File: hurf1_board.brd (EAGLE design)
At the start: 160 x 100 mm, 32 parts, among them IC1 STM32F10XCXT6, J1 0R, J2 0R, X1 MINI-USB-32005-201, Y1 8MHz

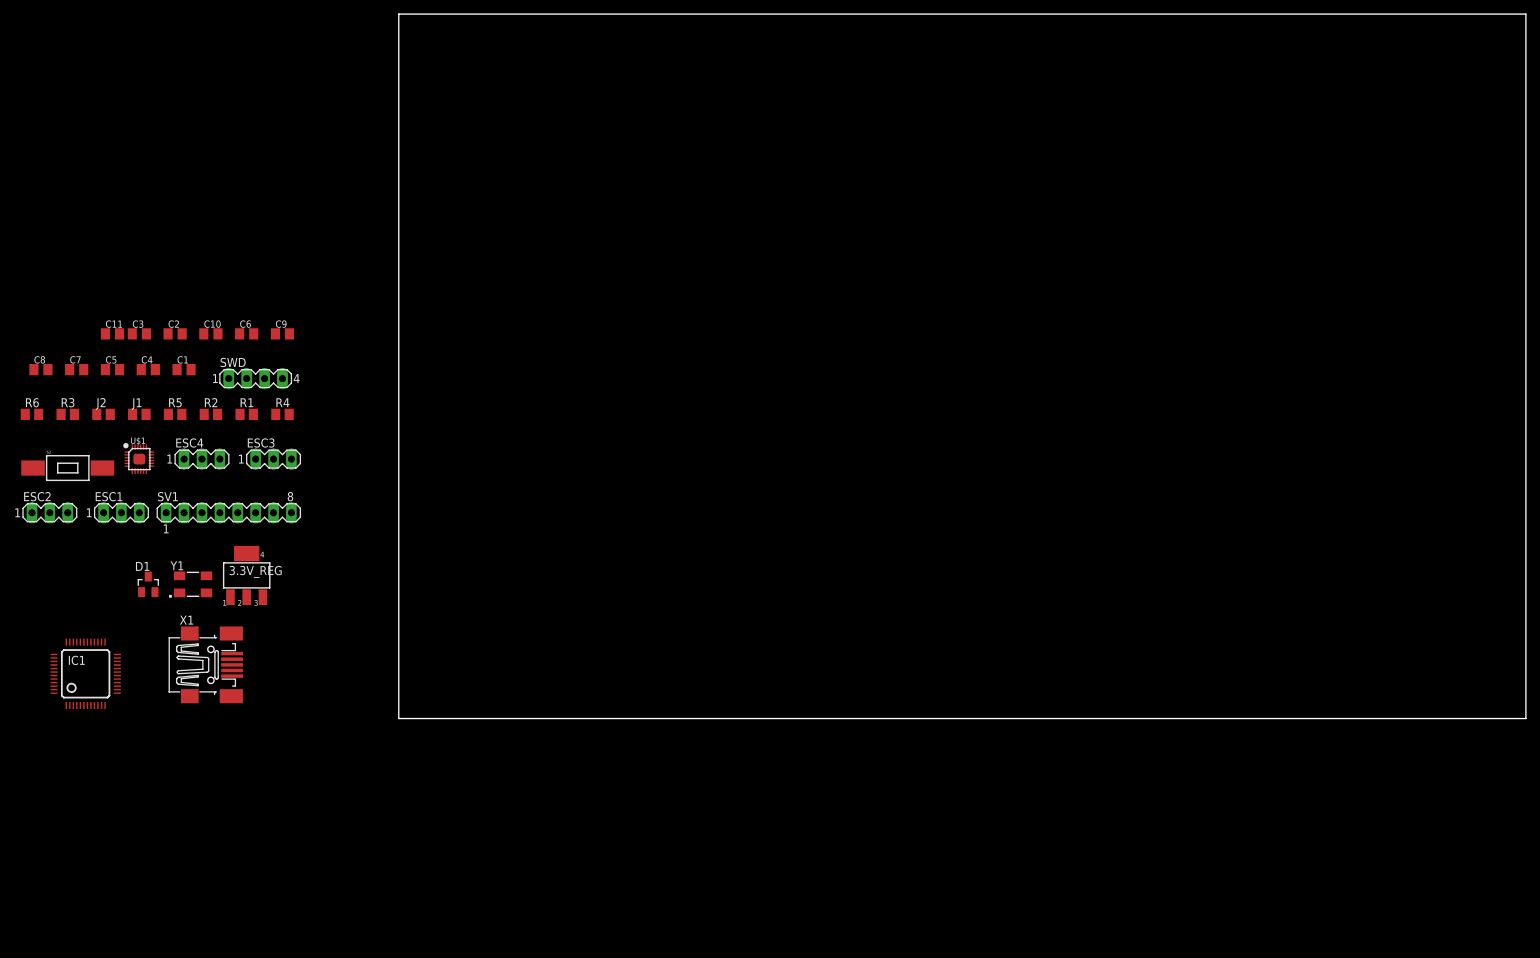
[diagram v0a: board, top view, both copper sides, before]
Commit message: Schematic Completed -schematic w1 -board w1 -controlboard sketch added (.dxf) =.gitignore updated = hurf1_schematic.sch -> hurf1_board.sch = board images added
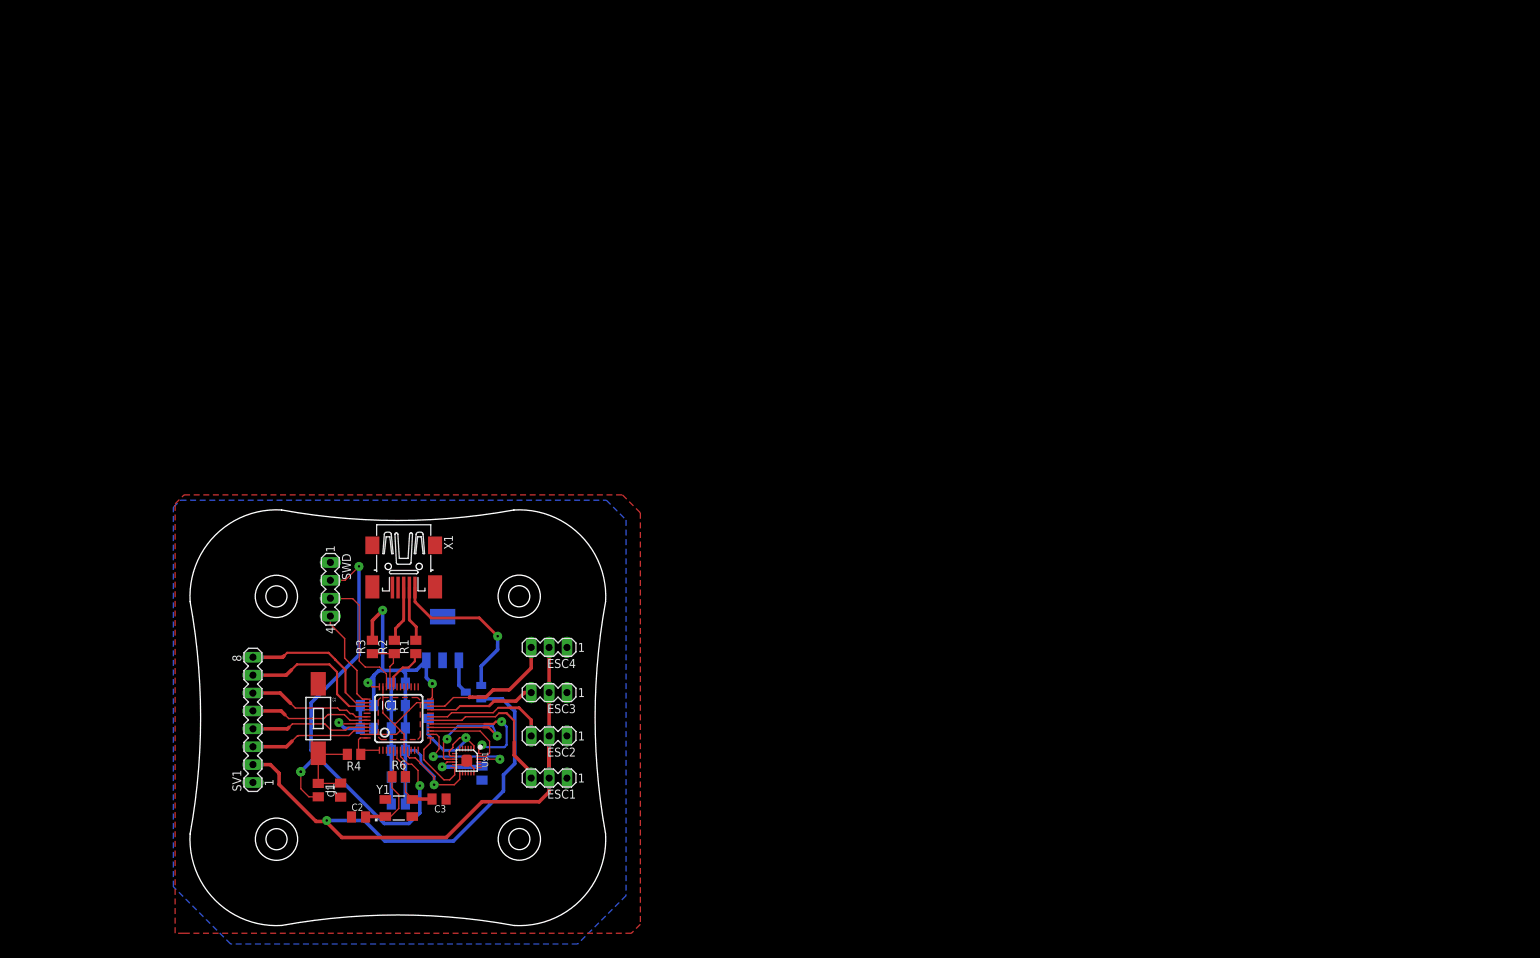
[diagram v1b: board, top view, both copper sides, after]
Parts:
- moved C8 79.8 mm to (-0.06, -12.1), flipped to the bottom, turned to 180 degrees
- moved C3 78.6 mm to (5.71, -11.4), turned to 180 degrees
- moved ESC2 77.6 mm to (21.3, -2.48), turned to 180 degrees
- moved C4 74.3 mm to (11.8, -7.75), flipped to the bottom, turned to 270 degrees
- moved C7 73.7 mm to (-0.06, -8.32), flipped to the bottom, turned to 180 degrees
- moved C2 73.4 mm to (-5.71, -14.0)
- moved R6 73.2 mm to (0.00, -8.26)
- moved ESC1 71.4 mm to (21.3, -8.45), turned to 180 degrees
- moved C11 69.1 mm to (-0.06, -1.33), flipped to the bottom, turned to 180 degrees
- moved C5 67.6 mm to (-0.06, -4.51), flipped to the bottom
- moved C1 63.7 mm to (-8.26, -10.2), turned to 90 degrees
- moved U$1 63.2 mm to (9.65, -5.97), turned to 270 degrees
- moved C6 59.5 mm to (4.19, 1.02), flipped to the bottom, turned to 270 degrees
- moved C10 59.1 mm to (-0.06, 1.84), flipped to the bottom, turned to 180 degrees
- moved J1 59.1 mm to (-11.4, -10.2), turned to 270 degrees
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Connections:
- net SPI1_SS renamed SPI1_NSS
- net USB_N renamed USB_DM
- net USB_P renamed USB_DP
- net ESC1: now also IC1.18
- net ESC2: now also IC1.19
- net ESC3: now also IC1.21
- net ESC4: now also IC1.22
- net MPU_INT: now also IC1.13
- net RC_IN1: now also IC1.46
- net RC_IN2: now also IC1.45
- net RC_IN3: now also IC1.43
- net RC_IN4: now also IC1.42
- net RC_IN5: now also IC1.39
- net RC_IN6: now also IC1.38
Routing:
- net UNREG_5V: track 0.00 -> 123.3 mm, vias 0 -> 1
- net 3.3V: track 0.00 -> 97.4 mm, vias 0 -> 4
- net NRST: track 0.00 -> 73.0 mm, vias 0 -> 4
- net GND: track 0.00 -> 43.3 mm
- net USB_UNREG: track 0.00 -> 23.7 mm, vias 0 -> 1
- net SPI1_MISO: track 0.00 -> 23.5 mm, vias 0 -> 2
- net ESC1: track 0.00 -> 21.9 mm
- net RC_IN6: track 0.00 -> 21.3 mm
- net RC_IN5: track 0.00 -> 21.1 mm
- net ESC4: track 0.00 -> 19.5 mm
- net SPI1_MOSI: track 0.00 -> 19.0 mm, vias 0 -> 2
- net SWDIO: track 0.00 -> 18.9 mm
- net ESC2: track 0.00 -> 17.8 mm
- net VDDIO: track 0.00 -> 17.7 mm, vias 0 -> 1
- net RC_IN4: track 0.00 -> 17.6 mm
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- added copper zone on layer 1, net GND
- added copper zone on layer 16, net GND
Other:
- board size 160 x 100 mm -> 59 x 59 mm

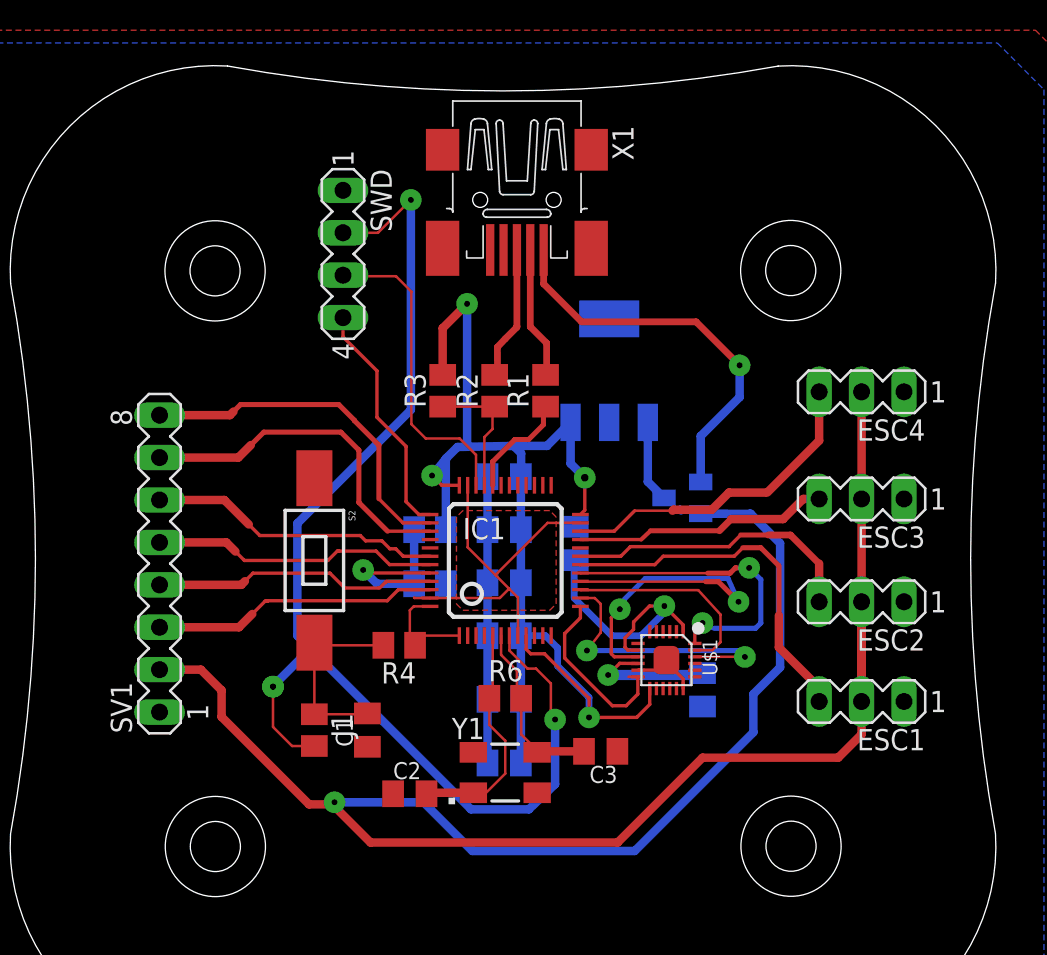
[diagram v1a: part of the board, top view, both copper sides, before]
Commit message: Circuit Size Shrinked -schematic w1 (updated) -board w1s1 (updated)  *SMD Package changed from 0805 -> 0603  *SWD Port changed from DIL -> JST-SH  X UNREG_5V pin must be connected to diode
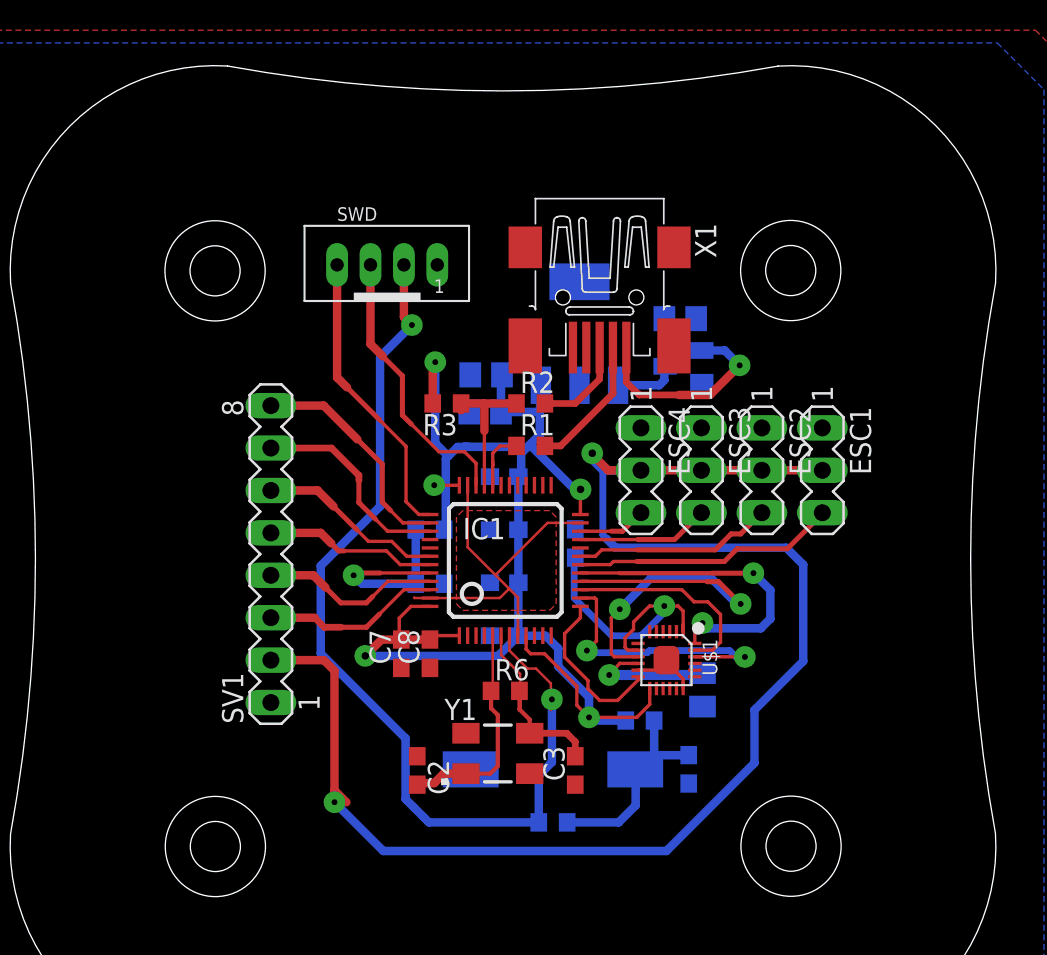
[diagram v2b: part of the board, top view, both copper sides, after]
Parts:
- added C12, C13, C14: 10uF, rcl:C0805
- C1, C10, C11, C2, C3, C5, C6, C7, C8, C9: device resistor:C0805K -> rcl:C0603
- J1, J2, R1, R2, R3, R4, R5, R6: device adafruit:M0805 -> rcl:R0603
- SWD: device con-lstb:MA04-1 -> SRG:JST_B4B-PH_HEADER
- moved C1 19.4 mm to (11.0, -12.5), flipped to the bottom
- moved S2 19.0 mm to (2.86, -12.5), flipped to the bottom, turned to 180 degrees
- moved J1 15.3 mm to (2.86, -15.7), flipped to the bottom, turned to 0 degrees
- moved R4 15.1 mm to (8.06, -9.59), flipped to the bottom
- moved ESC1 14.0 mm to (19.0, 5.40), turned to 270 degrees
- moved ESC4 14.0 mm to (8.13, 5.40), turned to 270 degrees
- moved ESC2 9.88 mm to (15.4, 5.40), turned to 270 degrees
- moved ESC3 9.74 mm to (11.7, 5.40), turned to 270 degrees
- moved C8 7.91 mm to (-4.51, -5.59), flipped to the top, turned to 90 degrees
- moved D1 7.87 mm to (10.7, 11.6)
- moved X1 7.66 mm to (5.65, 15.7)
- moved C7 6.74 mm to (-6.22, -5.59), flipped to the top, turned to 90 degrees
- moved SV1 6.69 mm to (-14.0, 0.38)
- moved R1 3.42 mm to (1.52, 6.86), turned to 0 degrees
- moved 3.3V_REG 2.85 mm to (4.45, 13.6)
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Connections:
- net 3.3V: now also C12.1, C13.1
- net GND: now also C12.2, C13.2, C14.2, SWD.P1; no longer SWD.1
- net N$4: now also C14.1
- net NRST: now also SWD.P2; no longer SWD.2
- net SWDCLK: now also SWD.P4; no longer SWD.4
- net SWDIO: now also SWD.P3; no longer SWD.3
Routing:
- net UNREG_5V: track 123.3 -> 88.3 mm, vias 1 -> 2
- net GND: track 43.3 -> 26.1 mm
- net ESC4: track 19.5 -> 4.09 mm
- net NRST: track 73.0 -> 59.2 mm, vias 4 -> 2
- net USB_UNREG: track 23.7 -> 12.5 mm
- net RC_IN5: track 21.1 -> 12.5 mm
- net RC_IN6: track 21.3 -> 13.8 mm
- net ESC3: track 15.3 -> 7.91 mm
- net N$2: track 12.7 -> 5.77 mm
- net RC_IN3: track 17.2 -> 10.4 mm
- net RC_IN4: track 17.6 -> 11.2 mm
- net RC_IN1: track 17.1 -> 10.7 mm
- net RC_IN2: track 17.0 -> 10.8 mm
- net ESC1: track 21.9 -> 15.8 mm
- net ESC2: track 17.8 -> 11.9 mm
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
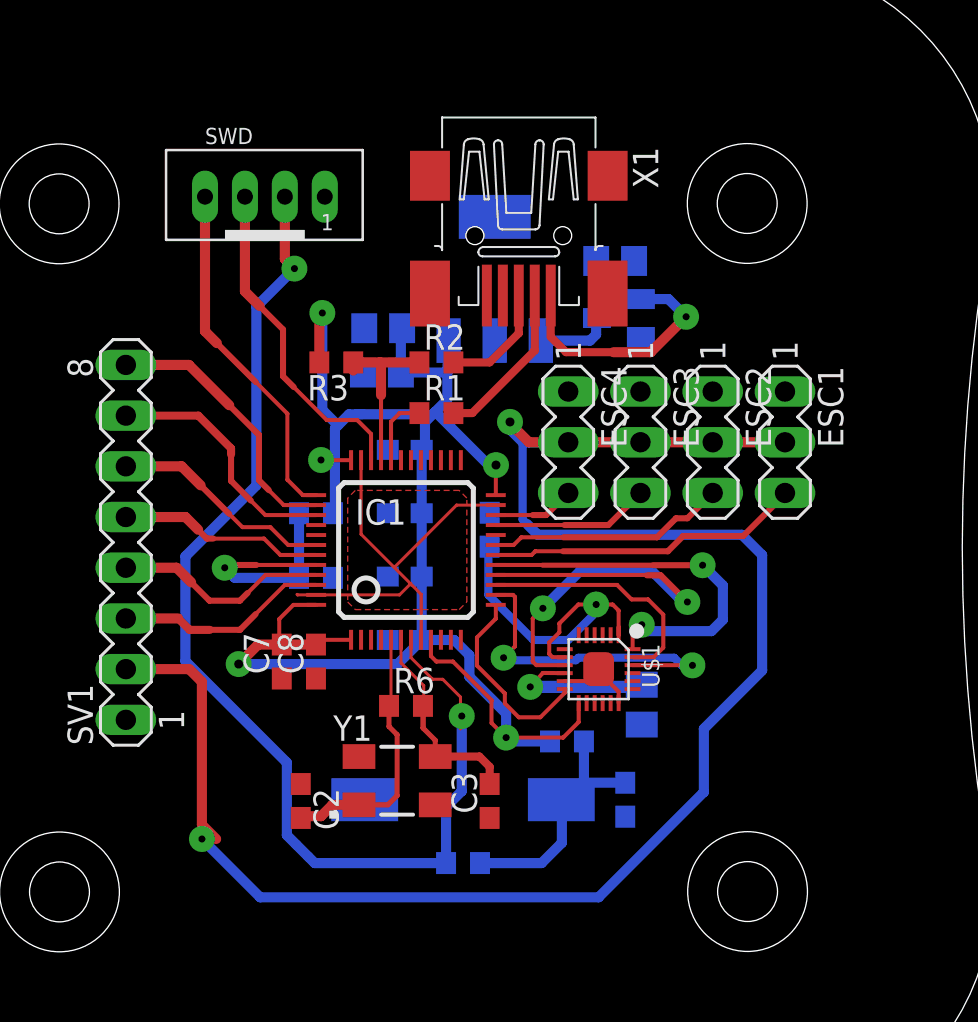
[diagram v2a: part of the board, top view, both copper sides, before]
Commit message: Circuit Design Updated  -schematic w1(updated)   *1x Power Led , 2x Status Led Added   *RC_OUT and SWD packages updated  -board w1s1 (updated)   *All connections solved   *Schematic changes applied   X* RC_IN port MUST be updated from DIL -> JST-SH 8 Pin
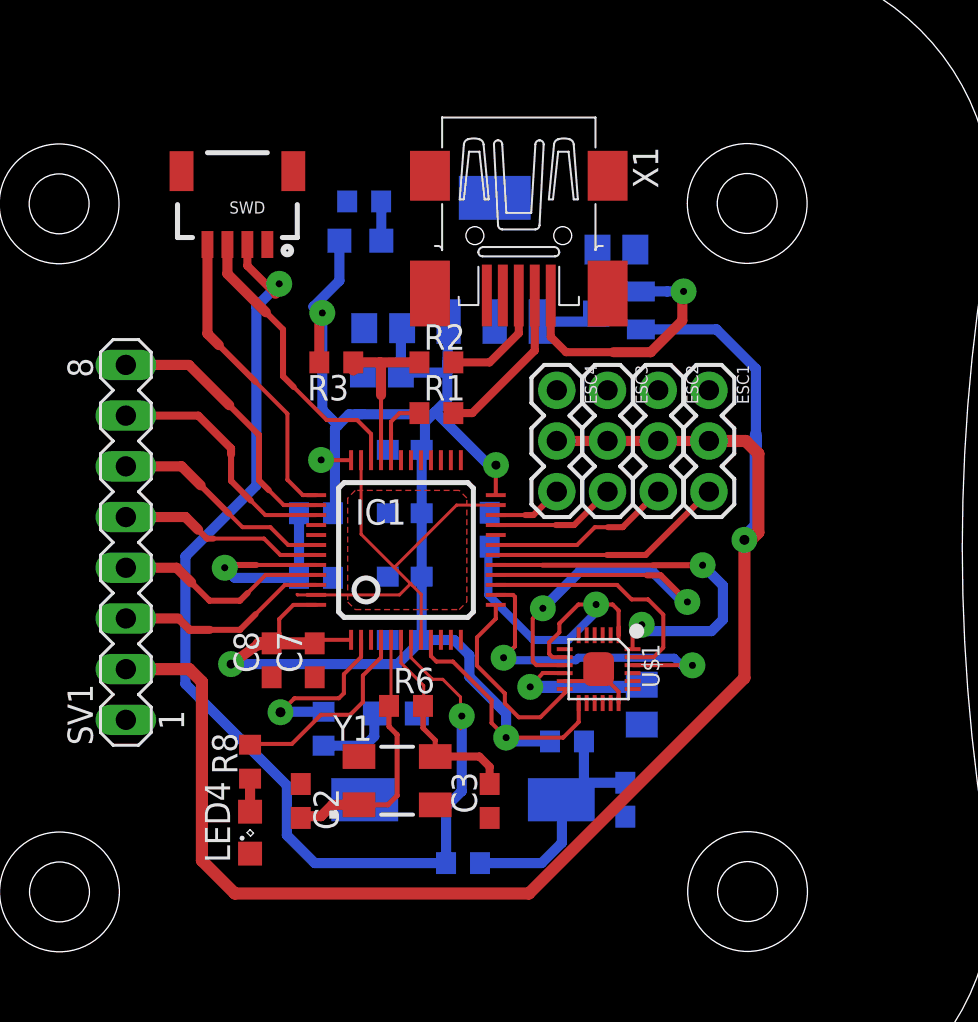
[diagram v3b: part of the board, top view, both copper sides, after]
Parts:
- added LED4, LED5, LED6: (no value), led:SML0805
- added R7, R8, R9: 330R, rcl:R0603
- ESC1: value rotor_lf -> (none); device con-lstb:MA03-1 -> SparkFun-Connectors:1X03
- ESC2: value rotor_rf -> (none); device con-lstb:MA03-1 -> SparkFun-Connectors:1X03
- ESC3: value rotor_rb -> (none); device con-lstb:MA03-1 -> SparkFun-Connectors:1X03
- ESC4: value rotor_lb -> (none); device con-lstb:MA03-1 -> SparkFun-Connectors:1X03
- SWD: device SRG:JST_B4B-PH_HEADER -> SparkFun-Connectors:1X04_1MM_RA
- moved ESC1 4.61 mm to (15.2, 8.00)
- moved ESC2 3.77 mm to (12.6, 8.00)
- moved ESC3 3.08 mm to (10.1, 8.00)
- moved SWD 2.73 mm to (-8.45, 15.3), turned to 180 degrees
- moved ESC4 2.67 mm to (7.56, 8.00)
- moved C8 2.22 mm to (-6.73, -5.52)
- moved C7 1.65 mm to (-4.57, -5.52)
- moved 3.3V_REG 0.95 mm to (4.45, 14.5)
- moved C14 0.58 mm to (10.5, 15.0)
- moved D1 0.38 mm to (10.7, 12.0)
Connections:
- new net N$6: LED6.A, R9.1
- new net N$7: LED5.C, R7.1
- new net N$8: LED4.A, R8.1
- new net STATUS_LED1: IC1.2, R9.2
- new net STATUS_LED2: IC1.4, R8.2
- net 3.3V: now also LED5.A
- net GND: now also LED4.C, LED6.C, R7.2, SWD.1; no longer SWD.P1
- net NRST: now also SWD.2; no longer SWD.P2
- net SWDCLK: now also SWD.4; no longer SWD.P4
- net SWDIO: now also SWD.3; no longer SWD.P3
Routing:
- net STATUS_LED2: track 0.00 -> 10.0 mm
- net STATUS_LED1: track 0.00 -> 8.77 mm, vias 0 -> 1
- net UNREG_5V: track 88.3 -> 83.0 mm, vias 2 -> 1
- net 3.3V: track 98.8 -> 103.8 mm
- net N$6: track 0.00 -> 3.89 mm
- net ESC1: track 15.8 -> 12.0 mm
- net ESC2: track 11.9 -> 9.24 mm
- net SWDCLK: track 17.6 -> 15.2 mm
- net SWDIO: track 16.7 -> 14.7 mm
- net N$7: track 0.00 -> 1.97 mm
- net N$8: track 0.00 -> 1.66 mm
- net ESC3: track 7.91 -> 6.29 mm
- net NRST: track 59.2 -> 58.0 mm
- net N$4: track 6.60 -> 7.73 mm
- net USB_UNREG: track 12.5 -> 13.3 mm
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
